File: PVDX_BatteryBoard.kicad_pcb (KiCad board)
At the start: 2 copper layers, 75.7 x 115 mm, 44 parts, among them J1 Conn_01x19, J10 Conn_01x02_Pin, J11 Conn_01x01_Pin, J12 Conn_01x02, J2 Conn_01x06, J3 Conn_01x10, J4 Conn_01x02_Pin, J5 Conn_01x01_Pin, J6 Conn_01x02_Pin, J7 Conn_01x01_Pin, J8 Conn_01x02_Pin, J9 Conn_01x01_Pin, Q1 DMC2053UVT, Q2 DMC2053UVT

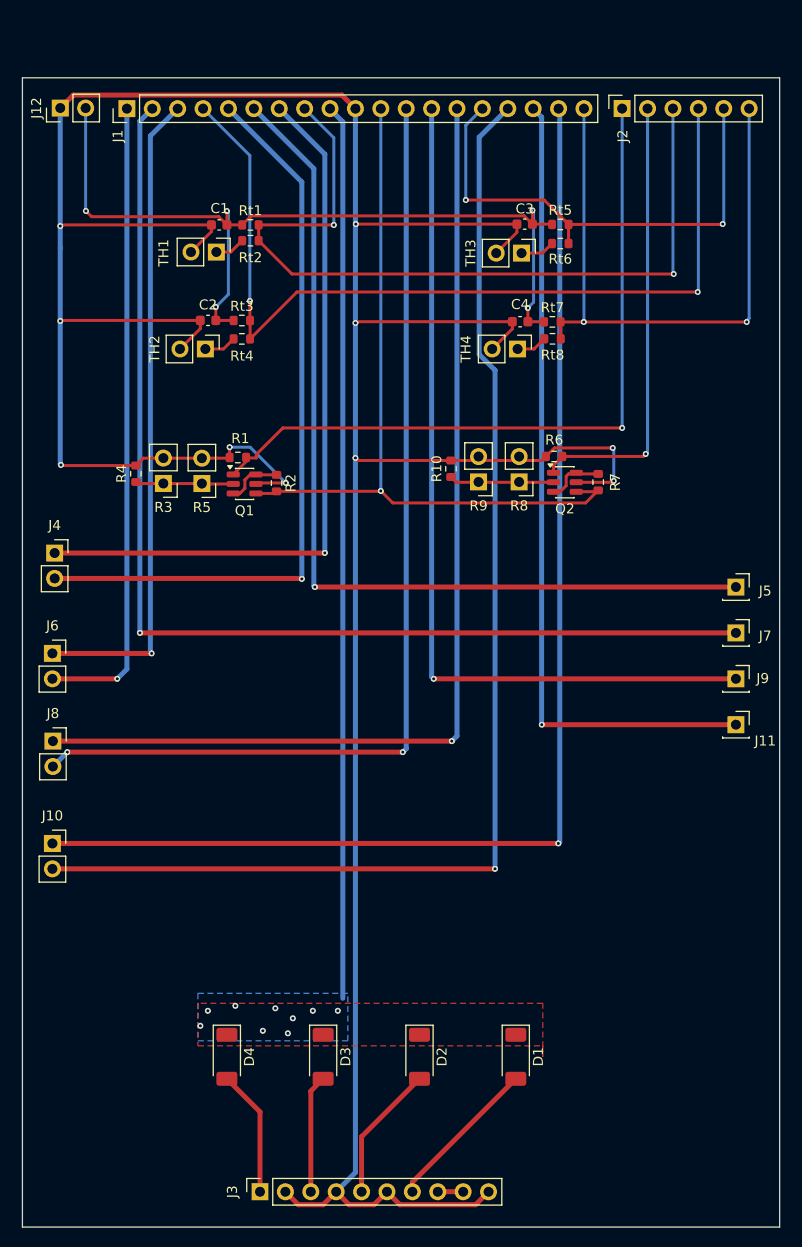
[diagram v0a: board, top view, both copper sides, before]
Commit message: updated board and designed reviewed by my coworkers
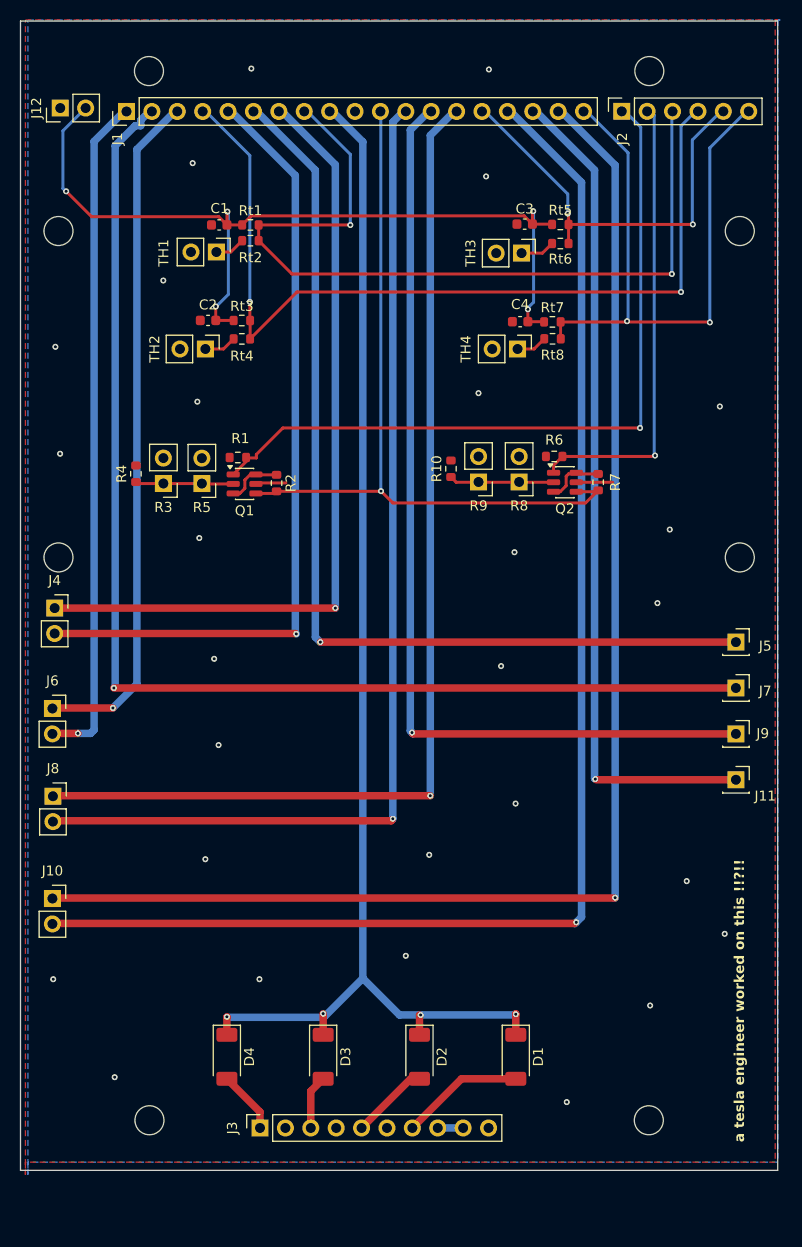
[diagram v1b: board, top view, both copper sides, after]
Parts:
- moved J3 6.38 mm to (127.2, 141.7)
- moved J11 5.51 mm to (174.8, 106.9)
- moved J4 5.51 mm to (106.7, 89.7)
- moved J5 5.51 mm to (174.8, 93.1)
- moved J6 5.51 mm to (106.5, 99.8)
- moved J10 5.51 mm to (106.5, 118.8)
- moved J7 5.51 mm to (174.8, 97.7)
- moved J8 5.51 mm to (106.5, 108.5)
- moved J9 5.51 mm to (174.8, 102.3)
- moved J1 0.28 mm to (113.9, 40.0)
- moved J2 0.28 mm to (163.4, 40.0)
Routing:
- net SOLAR_1s_GND: track 337.4 -> 7.34 mm, vias 10 -> 28
- net SOLAR: track 89.5 -> 128.4 mm, vias 9 -> 4
- net BATT4+: track 122.2 -> 137.1 mm
- net BATT4-: track 124.2 -> 137.6 mm
- net BATT2M: track 112.6 -> 122.0 mm
- net BATT3M: track 87.3 -> 95.9 mm
- net NTC3: track 50.1 -> 42.3 mm
- net BATT1-: track 73.4 -> 80.4 mm
- net SOLAR_3s1: track 12.7 -> 6.29 mm
- net SOLAR_3s2: track 11.8 -> 5.43 mm
- net SOLAR_3s3: track 13.7 -> 7.83 mm
- net BATT3+: track 100.1 -> 105.5 mm, vias 2 -> 1
- net BATT1M: track 92.5 -> 97.7 mm
- net BATT1+: track 74.8 -> 79.4 mm
- net BATT3-: track 103.5 -> 107.6 mm
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- added copper zone on B.Cu, net SOLAR_1s_GND
- added copper zone on F.Cu, net SOLAR_1s_GND
- removed copper zone on B.Cu, net SOLAR
- removed copper zone on F.Cu, net SOLAR
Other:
- outline, holes or cut-outs redrawn
- board text added: "USE THIS ONE!"
- board text added: "a tesla engineer worked on this !!?!!"
- board text added: "ever true :)"

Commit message: Add battery overdischarge & short protections to board
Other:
- board text added: "W/O BATT PROTECTION"
- board text removed: "USE THIS ONE!"
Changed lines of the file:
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@@
 		)
 	)
-	(gr_text "USE THIS ONE!"
-		(at 76.56 102.02 0)
+	(gr_text "W/O BATT PROTECTION"
+		(at 73 101.95 0)
 		(layer "Cmts.User")
 		(effects
